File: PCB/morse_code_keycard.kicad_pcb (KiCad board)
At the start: 2 copper layers, 85.6 x 54 mm, 50 parts, among them SW1 SW_Push, SW2 SW_Push, U1 CH32V203GxUx

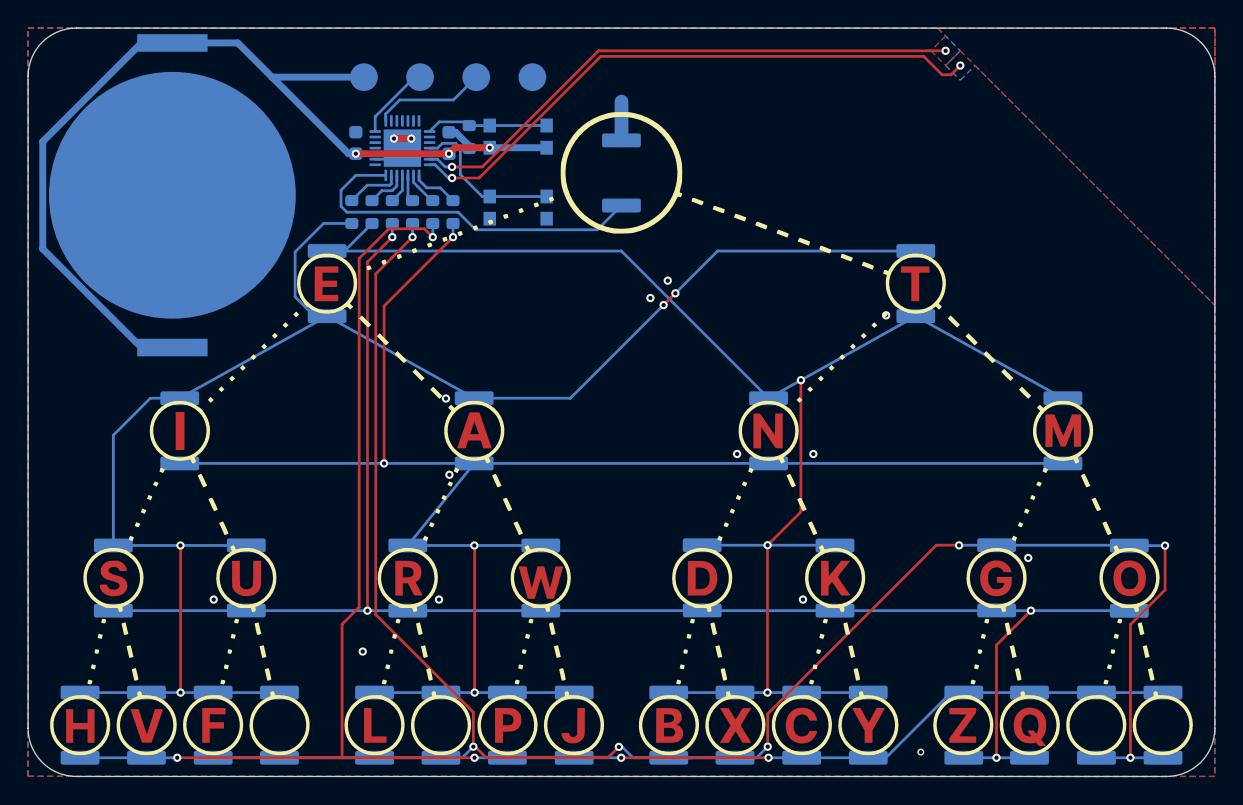
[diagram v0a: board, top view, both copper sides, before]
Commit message: updated PCB with thicker traces and  other improvements + New pcb image
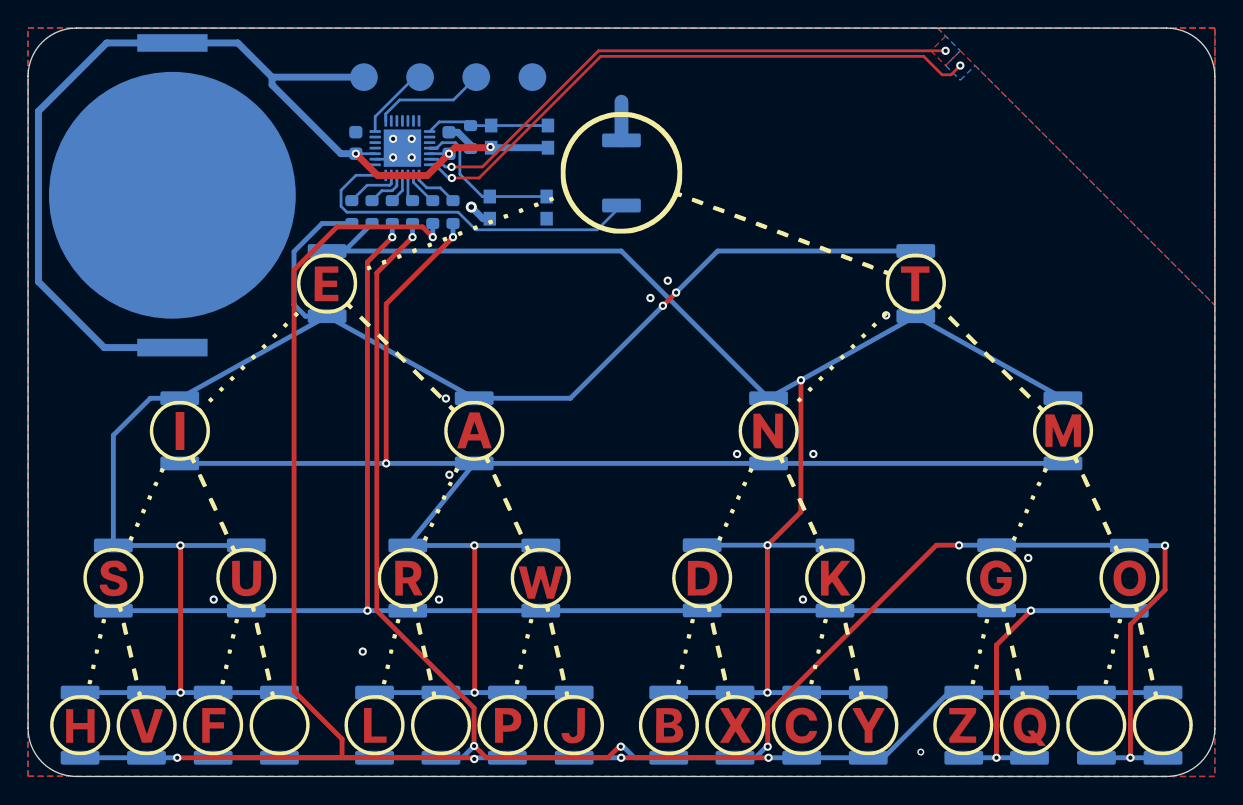
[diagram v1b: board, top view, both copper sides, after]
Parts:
- moved R1 0.10 mm to (143.0, 67.4)
- moved SW2 0.10 mm to (146.6, 67.4)
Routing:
- net Net-(D14-A): track 124.0 -> 129.3 mm
- net +3V3: track 72.2 -> 77.3 mm
- net Net-(D13-A): track 143.9 -> 140.6 mm
- net GND: track 8.39 -> 9.04 mm, vias 15 -> 18
- net /~{RST}: track 11.3 -> 11.9 mm
- net Net-(D1-K): track 121.1 -> 121.6 mm
